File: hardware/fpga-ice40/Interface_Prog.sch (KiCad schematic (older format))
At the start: 2 parts, among them J6 Conn_02x05_Odd_Even, J7 Conn_02x05_Odd_Even

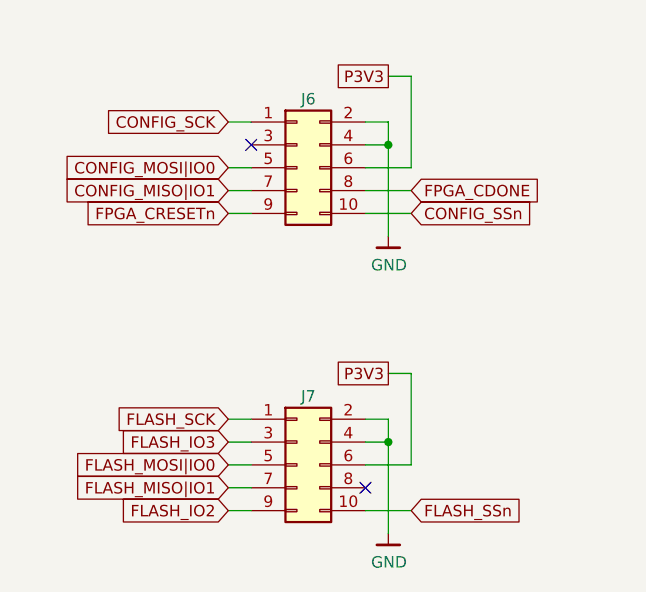
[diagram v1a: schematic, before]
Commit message: Reannotate schematic symbols
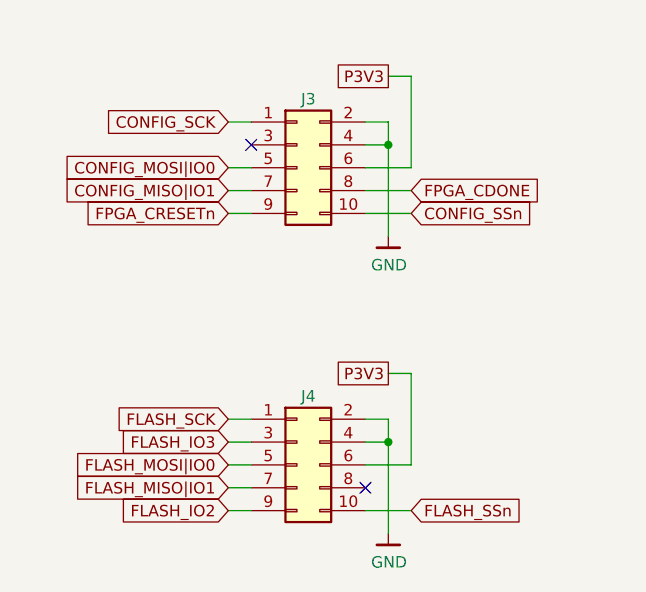
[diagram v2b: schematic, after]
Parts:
- renumbered J6 to J3, J7 to J4
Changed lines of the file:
@@
 P 5850 4150
 AR Path="/5F90AA21" Ref="#PWR?"  Part="1"
-AR Path="/5F8FED6E/5F90AA21" Ref="#PWR0119"  Part="1"
-F 0 "#PWR0119" H 5850 3900 50  0001 C CNN
+AR Path="/5F8FED6E/5F90AA21" Ref="#PWR019"  Part="1"
+F 0 "#PWR019" H 5850 3900 50  0001 C CNN
 F 1 "GND" H 5853 4024 50  0000 C CNN
 F 2 "" H 5750 3800 50  0001 C CNN
@@
 P 5450 3850
 AR Path="/5F90AA27" Ref="J?"  Part="1"
-AR Path="/5F8FED6E/5F90AA27" Ref="J6"  Part="1"
-F 0 "J6" H 5500 4150 50  0000 C CNN
+AR Path="/5F8FED6E/5F90AA27" Ref="J3"  Part="1"
+F 0 "J3" H 5500 4150 50  0000 C CNN
 F 1 "Conn_02x05_Odd_Even" H 5500 4176 50  0001 C CNN
 F 2 "ng_conn:Samtec_FTSH-105-XX-X-DV-Mating" H 5450 3850 50  0001 C CNN
@@
 P 5450 5150
 AR Path="/5F90AA2D" Ref="J?"  Part="1"
-AR Path="/5F8FED6E/5F90AA2D" Ref="J7"  Part="1"
-F 0 "J7" H 5500 5450 50  0000 C CNN
+AR Path="/5F8FED6E/5F90AA2D" Ref="J4"  Part="1"
+F 0 "J4" H 5500 5450 50  0000 C CNN
 F 1 "Conn_02x05_Odd_Even" H 5500 5476 50  0001 C CNN
 F 2 "ng_conn:Samtec_FTSH-105-XX-X-DV-Mating" H 5450 5150 50  0001 C CNN
@@
 P 5850 5450
 AR Path="/5F90AA41" Ref="#PWR?"  Part="1"
-AR Path="/5F8FED6E/5F90AA41" Ref="#PWR0120"  Part="1"
-F 0 "#PWR0120" H 5850 5200 50  0001 C CNN
+AR Path="/5F8FED6E/5F90AA41" Ref="#PWR020"  Part="1"
+F 0 "#PWR020" H 5850 5200 50  0001 C CNN
 F 1 "GND" H 5853 5324 50  0000 C CNN
 F 2 "" H 5750 5100 50  0001 C CNN

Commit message: Flash programming header can hold FPGA in configuration reset
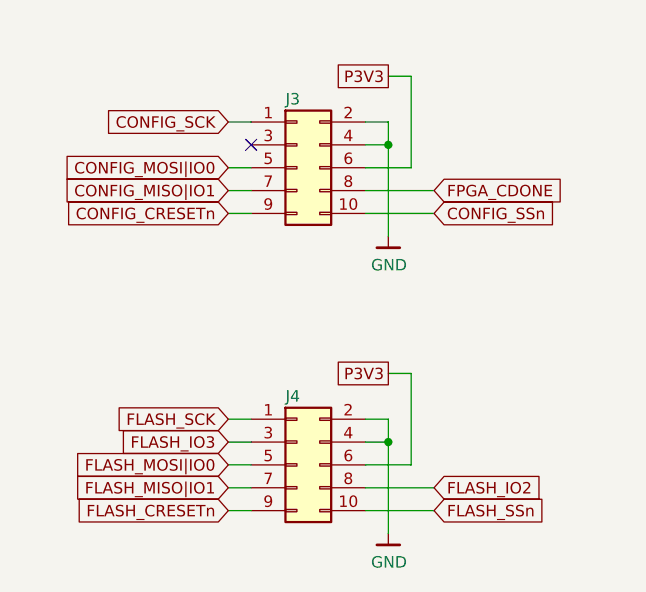
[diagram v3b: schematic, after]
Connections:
- net FLASH_IO2: now also J4.8 (Pin_8); no longer J4.9 (Pin_9)
- net FPGA_CRESETn renamed CONFIG_CRESETn
- new net FLASH_CRESETn: J4.9 (Pin_9)
- no-connect marks 2 -> 1
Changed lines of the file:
@@
 $EndDescr
 Wire Wire Line
-	5750 3950 5950 3950
+	5750 3950 6050 3950
 Wire Wire Line
 	5250 4050 5150 4050
@@
 	5250 3650 5150 3650
 Wire Wire Line
-	5750 4050 5950 4050
-Text GLabel 5950 3950 2    50   Input ~ 0
+	5750 4050 6050 4050
+Text GLabel 6050 3950 2    50   Input ~ 0
 FPGA_CDONE
-Text GLabel 5150 4050 0    50   Input ~ 0
-FPGA_CRESETn
 Text GLabel 5150 3850 0    50   Input ~ 0
 CONFIG_MOSI|IO0
@@
 Text GLabel 5150 3650 0    50   Input ~ 0
 CONFIG_SCK
-Text GLabel 5950 4050 2    50   Input ~ 0
+Text GLabel 6050 4050 2    50   Input ~ 0
 CONFIG_SSn
-Text GLabel 5950 5350 2    50   Input ~ 0
+Text GLabel 6050 5350 2    50   Input ~ 0
 FLASH_SSn
 Text GLabel 5150 4950 0    50   Input ~ 0
@@
 AR Path="/5F90AA27" Ref="J?"  Part="1"
 AR Path="/5F8FED6E/5F90AA27" Ref="J3"  Part="1"
-F 0 "J3" H 5500 4150 50  0000 C CNN
+F 0 "J3" H 5400 4150 50  0000 L CNN
 F 1 "Conn_02x05_Odd_Even" H 5500 4176 50  0001 C CNN
 F 2 "ng_conn:Samtec_FTSH-105-XX-X-DV-Mating" H 5450 3850 50  0001 C CNN
@@
 AR Path="/5F90AA2D" Ref="J?"  Part="1"
 AR Path="/5F8FED6E/5F90AA2D" Ref="J4"  Part="1"
-F 0 "J4" H 5500 5450 50  0000 C CNN
+F 0 "J4" H 5400 5450 50  0000 L CNN
 F 1 "Conn_02x05_Odd_Even" H 5500 5476 50  0001 C CNN
 F 2 "ng_conn:Samtec_FTSH-105-XX-X-DV-Mating" H 5450 5150 50  0001 C CNN
@@
 	5250 4950 5150 4950
 Wire Wire Line
-	5750 5350 5950 5350
+	5750 5350 6050 5350
 Wire Wire Line
 	5850 4750 5950 4750
@@
 Wire Wire Line
 	5950 4750 5950 5150
-NoConn ~ 5750 5250
 Wire Wire Line
 	5250 5350 5150 5350
-Text GLabel 5150 5350 0    50   Input ~ 0
+Text GLabel 6050 5250 2    50   Input ~ 0
 FLASH_IO2
 Wire Wire Line
@@
 Text GLabel 5150 5050 0    50   Input ~ 0
 FLASH_IO3
+Text GLabel 5150 5350 0    50   Input ~ 0
+FLASH_CRESETn
+Text GLabel 5150 4050 0    50   Input ~ 0
+CONFIG_CRESETn
+Wire Wire Line
+	5750 5250 6050 5250
 $EndSCHEMATC

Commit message: Component selection by MPN and routing cleanup
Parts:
- J3, J4: value Conn_02x05_Odd_Even -> FTSH-105-01-L-DV-K; MPN (none) -> FTSH-105-01-L-DV-K
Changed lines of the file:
@@
 AR Path="/5F8FED6E/5F90AA27" Ref="J3"  Part="1"
 F 0 "J3" H 5400 4150 50  0000 L CNN
-F 1 "Conn_02x05_Odd_Even" H 5500 4176 50  0001 C CNN
+F 1 "FTSH-105-01-L-DV-K" H 5500 4176 50  0001 C CNN
 F 2 "ng_conn:Samtec_FTSH-105-XX-X-DV-Mating" H 5450 3850 50  0001 C CNN
 F 3 "~" H 5450 3850 50  0001 C CNN
+F 4 "FTSH-105-01-L-DV-K" H 5450 3850 50  0001 C CNN "MPN"
 	1    5450 3850
 	1    0    0    -1
@@
 AR Path="/5F8FED6E/5F90AA2D" Ref="J4"  Part="1"
 F 0 "J4" H 5400 5450 50  0000 L CNN
-F 1 "Conn_02x05_Odd_Even" H 5500 5476 50  0001 C CNN
+F 1 "FTSH-105-01-L-DV-K" H 5500 5476 50  0001 C CNN
 F 2 "ng_conn:Samtec_FTSH-105-XX-X-DV-Mating" H 5450 5150 50  0001 C CNN
 F 3 "~" H 5450 5150 50  0001 C CNN
+F 4 "FTSH-105-01-L-DV-K" H 5450 5150 50  0001 C CNN "MPN"
 	1    5450 5150
 	1    0    0    -1

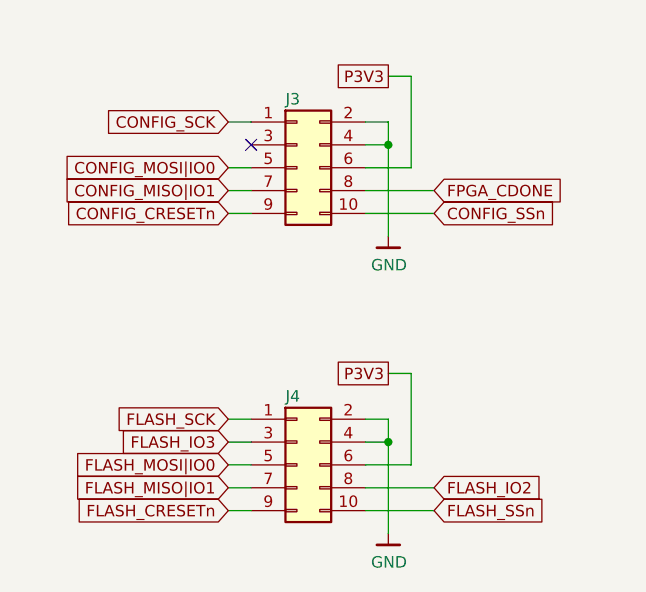
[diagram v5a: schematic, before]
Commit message: Standardize programming header pinouts for QSPI breakouts
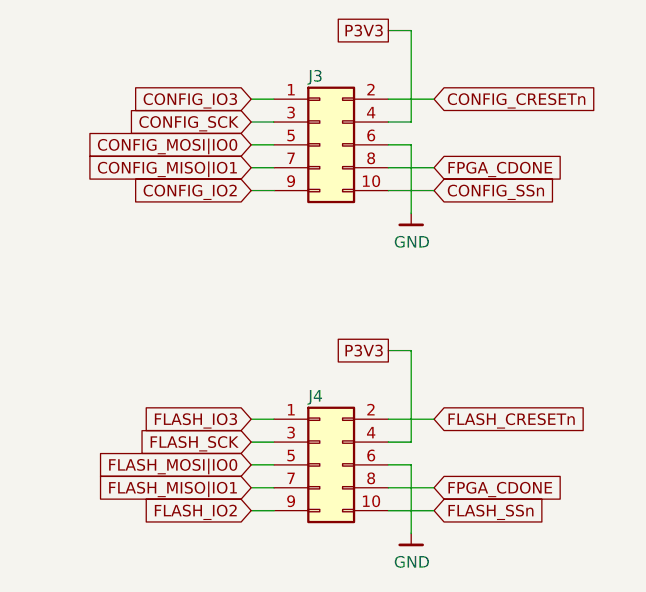
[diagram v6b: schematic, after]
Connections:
- net CONFIG_CRESETn: now also J3.2 (Pin_2); no longer J3.9 (Pin_9)
- net CONFIG_SCK: now also J3.3 (Pin_3); no longer J3.1 (Pin_1)
- net FLASH_CRESETn: now also J4.2 (Pin_2); no longer J4.9 (Pin_9)
- net FLASH_IO2: now also J4.9 (Pin_9); no longer J4.8 (Pin_8)
- net FLASH_IO3: now also J4.1 (Pin_1); no longer J4.3 (Pin_3)
- net FLASH_SCK: now also J4.3 (Pin_3); no longer J4.1 (Pin_1)
- net FPGA_CDONE: now also J4.8 (Pin_8)
- net GND: now also J3.6 (Pin_6), J4.6 (Pin_6); no longer J3.2 (Pin_2), J3.4 (Pin_4), J4.2 (Pin_2), J4.4 (Pin_4)
- net P3V3: now also J3.4 (Pin_4), J4.4 (Pin_4); no longer J3.6 (Pin_6), J4.6 (Pin_6)
- new net CONFIG_IO2: J3.9 (Pin_9)
- new net CONFIG_IO3: J3.1 (Pin_1)
- no-connect marks 1 -> 0
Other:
- moved on the sheet: J3, J4
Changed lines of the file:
@@
 $EndDescr
 Wire Wire Line
-	5750 3950 6050 3950
+	5850 3850 6050 3850
 Wire Wire Line
-	5250 4050 5150 4050
+	5850 3550 6050 3550
 Wire Wire Line
-	5250 3950 5150 3950
+	5350 3850 5250 3850
 Wire Wire Line
-	5250 3850 5150 3850
+	5350 3750 5250 3750
 Wire Wire Line
-	5250 3650 5150 3650
+	5350 3650 5250 3650
 Wire Wire Line
-	5750 4050 6050 4050
+	5850 3950 6050 3950
+Text GLabel 6050 3850 2    50   Input ~ 0
+FPGA_CDONE
+Text GLabel 5250 3750 0    50   Input ~ 0
+CONFIG_MOSI|IO0
+Text GLabel 5250 3850 0    50   Input ~ 0
+CONFIG_MISO|IO1
+Text GLabel 5250 3650 0    50   Input ~ 0
+CONFIG_SCK
 Text GLabel 6050 3950 2    50   Input ~ 0
-FPGA_CDONE
-Text GLabel 5150 3850 0    50   Input ~ 0
-CONFIG_MOSI|IO0
-Text GLabel 5150 3950 0    50   Input ~ 0
-CONFIG_MISO|IO1
-Text GLabel 5150 3650 0    50   Input ~ 0
-CONFIG_SCK
-Text GLabel 6050 4050 2    50   Input ~ 0
 CONFIG_SSn
 Text GLabel 6050 5350 2    50   Input ~ 0
 FLASH_SSn
-Text GLabel 5150 4950 0    50   Input ~ 0
+Text GLabel 5250 5050 0    50   Input ~ 0
 FLASH_SCK
-Text GLabel 5150 5150 0    50   Input ~ 0
+Text GLabel 5250 5150 0    50   Input ~ 0
 FLASH_MOSI|IO0
-Text GLabel 5150 5250 0    50   Input ~ 0
+Text GLabel 5250 5250 0    50   Input ~ 0
 FLASH_MISO|IO1
 Wire Wire Line
-	5850 3450 5950 3450
-Text GLabel 5850 3450 0    50   UnSpc ~ 0
+	5850 3250 5950 3250
+Text GLabel 5850 3250 0    50   UnSpc ~ 0
 P3V3
 $Comp
 L ng_power:GND #PWR?
 U 1 1 5F90AA21
-P 5850 4150
+P 5950 4050
 AR Path="/5F90AA21" Ref="#PWR?"  Part="1"
 AR Path="/5F8FED6E/5F90AA21" Ref="#PWR019"  Part="1"
-F 0 "#PWR019" H 5850 3900 50  0001 C CNN
-F 1 "GND" H 5853 4024 50  0000 C CNN
-F 2 "" H 5750 3800 50  0001 C CNN
-F 3 "" H 5850 4150 50  0001 C CNN
-	1    5850 4150
+F 0 "#PWR019" H 5950 3800 50  0001 C CNN
+F 1 "GND" H 5953 3924 50  0000 C CNN
+F 2 "" H 5850 3700 50  0001 C CNN
+F 3 "" H 5950 4050 50  0001 C CNN
+	1    5950 4050
 	1    0    0    -1
 $EndComp
@@
 L Connector_Generic:Conn_02x05_Odd_Even J?
 U 1 1 5F90AA27
-P 5450 3850
+P 5550 3750
 AR Path="/5F90AA27" Ref="J?"  Part="1"
 AR Path="/5F8FED6E/5F90AA27" Ref="J3"  Part="1"
-F 0 "J3" H 5400 4150 50  0000 L CNN
-F 1 "FTSH-105-01-L-DV-K" H 5500 4176 50  0001 C CNN
-F 2 "ng_conn:Samtec_FTSH-105-XX-X-DV-Mating" H 5450 3850 50  0001 C CNN
-F 3 "~" H 5450 3850 50  0001 C CNN
-F 4 "FTSH-105-01-L-DV-K" H 5450 3850 50  0001 C CNN "MPN"
-	1    5450 3850
+F 0 "J3" H 5500 4050 50  0000 L CNN
+F 1 "FTSH-105-01-L-DV-K" H 5600 4076 50  0001 C CNN
+F 2 "ng_conn:Samtec_FTSH-105-XX-X-DV-Mating" H 5550 3750 50  0001 C CNN
+F 3 "~" H 5550 3750 50  0001 C CNN
+F 4 "FTSH-105-01-L-DV-K" H 5550 3750 50  0001 C CNN "MPN"
+	1    5550 3750
 	1    0    0    -1
 $EndComp
@@
 L Connector_Generic:Conn_02x05_Odd_Even J?
 U 1 1 5F90AA2D
-P 5450 5150
+P 5550 5150
 AR Path="/5F90AA2D" Ref="J?"  Part="1"
 AR Path="/5F8FED6E/5F90AA2D" Ref="J4"  Part="1"
-F 0 "J4" H 5400 5450 50  0000 L CNN
-F 1 "FTSH-105-01-L-DV-K" H 5500 5476 50  0001 C CNN
-F 2 "ng_conn:Samtec_FTSH-105-XX-X-DV-Mating" H 5450 5150 50  0001 C CNN
-F 3 "~" H 5450 5150 50  0001 C CNN
-F 4 "FTSH-105-01-L-DV-K" H 5450 5150 50  0001 C CNN "MPN"
-	1    5450 5150
+F 0 "J4" H 5500 5450 50  0000 L CNN
+F 1 "FTSH-105-01-L-DV-K" H 5600 5476 50  0001 C CNN
+F 2 "ng_conn:Samtec_FTSH-105-XX-X-DV-Mating" H 5550 5150 50  0001 C CNN
+F 3 "~" H 5550 5150 50  0001 C CNN
+F 4 "FTSH-105-01-L-DV-K" H 5550 5150 50  0001 C CNN "MPN"
+	1    5550 5150
 	1    0    0    -1
 $EndComp
 Wire Wire Line
-	5750 3650 5850 3650
+	5950 3750 5950 4050
 Wire Wire Line
-	5850 3650 5850 3750
+	5950 3250 5950 3650
 Wire Wire Line
-	5750 3750 5850 3750
-Connection ~ 5850 3750
+	5350 5250 5250 5250
 Wire Wire Line
-	5850 3750 5850 4150
+	5350 5150 5250 5150
 Wire Wire Line
-	5750 3850 5950 3850
+	5350 5050 5250 5050
 Wire Wire Line
-	5950 3450 5950 3850
-NoConn ~ 5250 3750
-Wire Wire Line
-	5250 5250 5150 5250
-Wire Wire Line
-	5250 5150 5150 5150
-Wire Wire Line
-	5250 4950 5150 4950
-Wire Wire Line
-	5750 5350 6050 5350
-Wire Wire Line
-	5850 4750 5950 4750
-Text GLabel 5850 4750 0    50   UnSpc ~ 0
-P3V3
+	5850 5350 6050 5350
 $Comp
 L ng_power:GND #PWR?
 U 1 1 5F90AA41
-P 5850 5450
+P 5950 5450
 AR Path="/5F90AA41" Ref="#PWR?"  Part="1"
 AR Path="/5F8FED6E/5F90AA41" Ref="#PWR020"  Part="1"
-F 0 "#PWR020" H 5850 5200 50  0001 C CNN
-F 1 "GND" H 5853 5324 50  0000 C CNN
-F 2 "" H 5750 5100 50  0001 C CNN
-F 3 "" H 5850 5450 50  0001 C CNN
-	1    5850 5450
+F 0 "#PWR020" H 5950 5200 50  0001 C CNN
+F 1 "GND" H 5953 5324 50  0000 C CNN
+F 2 "" H 5850 5100 50  0001 C CNN
+F 3 "" H 5950 5450 50  0001 C CNN
+	1    5950 5450
 	1    0    0    -1
 $EndComp
 Wire Wire Line
-	5750 4950 5850 4950
-Wire Wire Line
-	5850 4950 5850 5050
-Wire Wire Line
-	5750 5050 5850 5050
-Connection ~ 5850 5050
-Wire Wire Line
-	5850 5050 5850 5450
-Wire Wire Line
-	5750 5150 5950 5150
-Wire Wire Line
-	5950 4750 5950 5150
-Wire Wire Line
-	5250 5350 5150 5350
-Text GLabel 6050 5250 2    50   Input ~ 0
+	5850 4950 6050 4950
+Text GLabel 5250 5350 0    50   Input ~ 0
 FLASH_IO2
 Wire Wire Line
-	5150 5050 5250 5050
-Text GLabel 5150 5050 0    50   Input ~ 0
+	5250 4950 5350 4950
+Text GLabel 5250 4950 0    50   Input ~ 0
 FLASH_IO3
-Text GLabel 5150 5350 0    50   Input ~ 0
+Text GLabel 6050 4950 2    50   Input ~ 0
 FLASH_CRESETn
-Text GLabel 5150 4050 0    50   Input ~ 0
+Text GLabel 6050 3550 2    50   Input ~ 0
 CONFIG_CRESETn
 Wire Wire Line
-	5750 5250 6050 5250
+	5850 5250 6050 5250
+Wire Wire Line
+	5350 3550 5250 3550
+Text GLabel 5250 3550 0    50   Input ~ 0
+CONFIG_IO3
+Wire Wire Line
+	5950 3750 5850 3750
+Wire Wire Line
+	5950 3650 5850 3650
+Wire Wire Line
+	5850 4650 5950 4650
+Wire Wire Line
+	5950 4650 5950 5050
+Wire Wire Line
+	5950 5050 5850 5050
+Wire Wire Line
+	5850 5150 5950 5150
+Wire Wire Line
+	5950 5150 5950 5450
+Text GLabel 5850 4650 0    50   UnSpc ~ 0
+P3V3
+Wire Wire Line
+	5350 3950 5250 3950
+Text GLabel 5250 3950 0    50   Input ~ 0
+CONFIG_IO2
+Wire Wire Line
+	5250 5350 5350 5350
+Text GLabel 6050 5250 2    50   Input ~ 0
+FPGA_CDONE
 $EndSCHEMATC
